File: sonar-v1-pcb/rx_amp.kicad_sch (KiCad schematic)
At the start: 13 parts, among them U301 Opamp_Dual

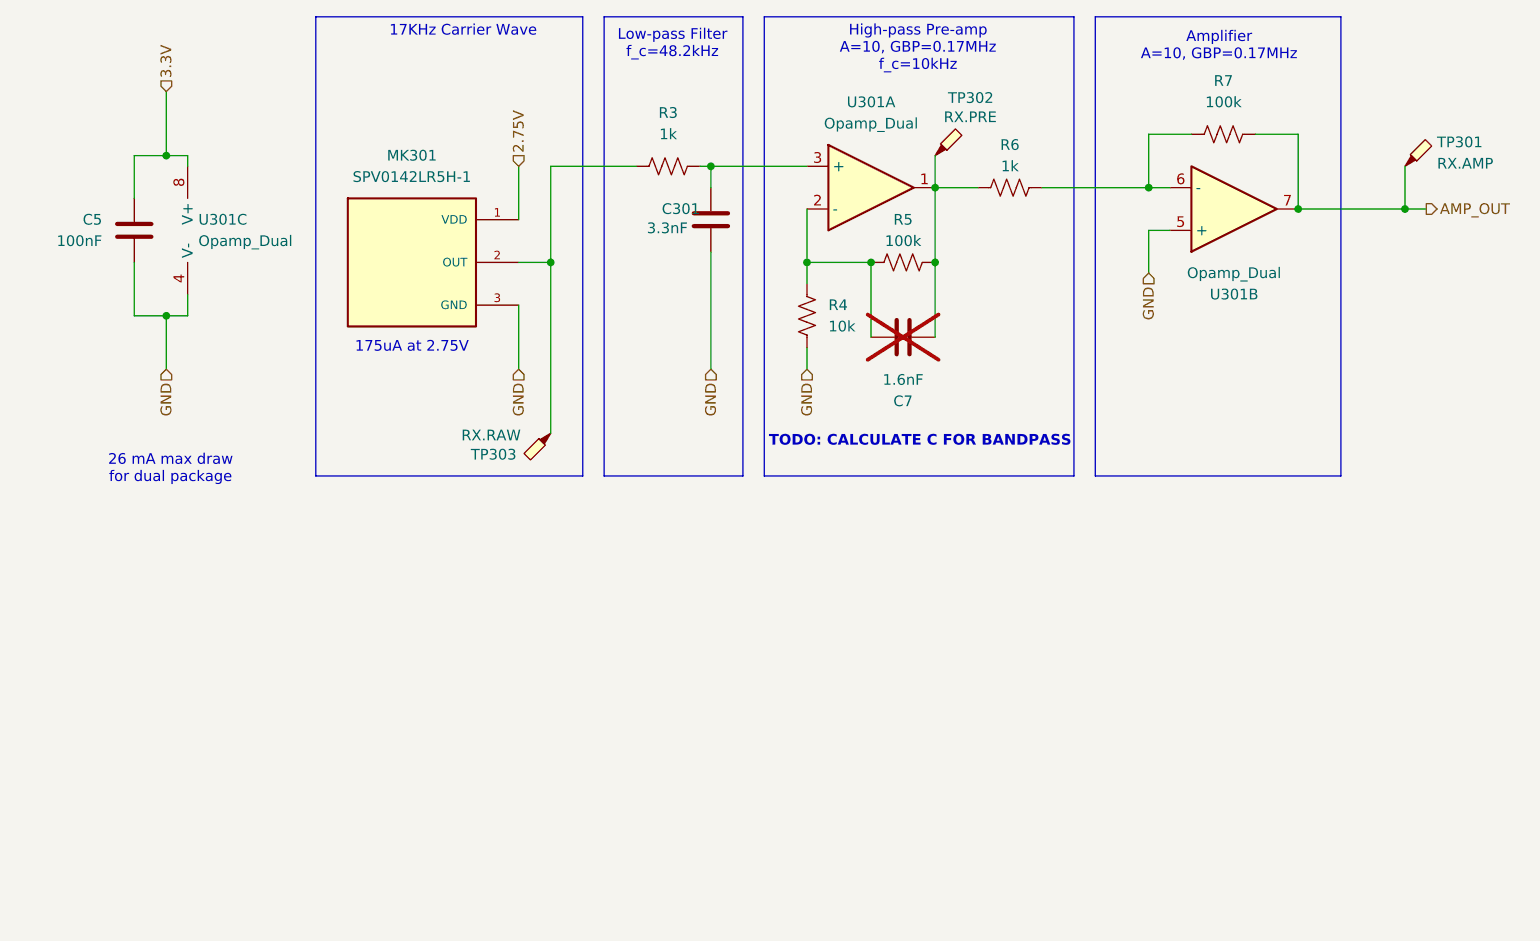
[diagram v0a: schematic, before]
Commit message: WIP hand-off: rx amp sim project, SPICE models, schematic updates
Adds rx_amp_sim KiCad project, SPICE models, Python setup-kicad.py
(replaces test_py.sh), CLAUDE.md, and a sweep of schematic edits across
the v1 board.

Co-Authored-By: Claude Opus 4.7 <noreply@anthropic.com>
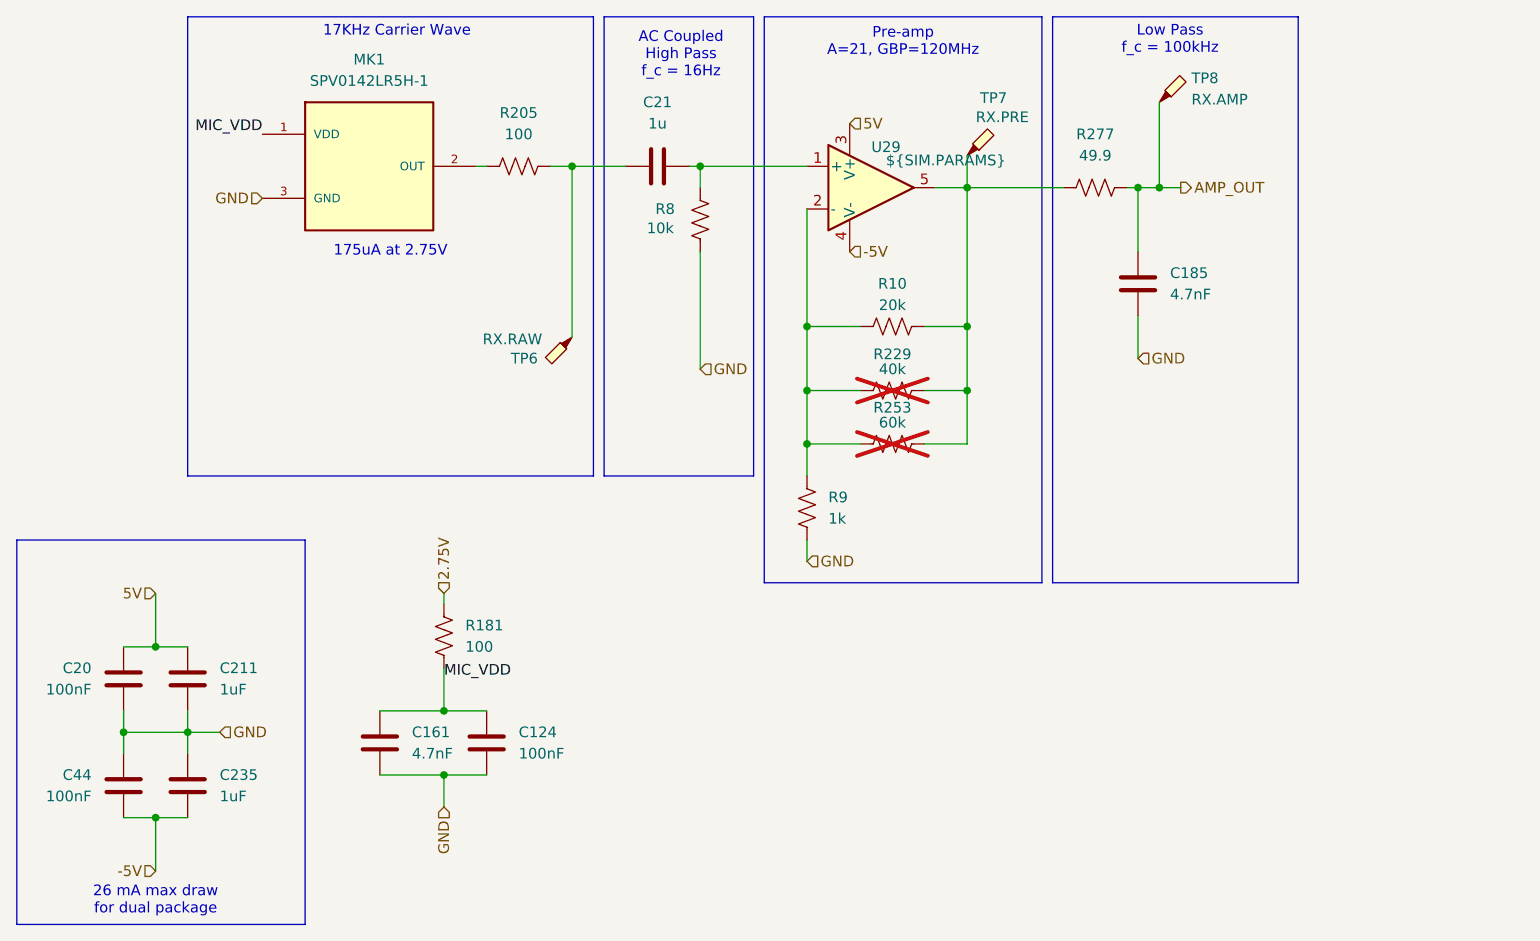
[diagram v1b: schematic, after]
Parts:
- removed C301: 3.3nF, Capacitor_SMD:C_0402_1005Metric, symbol Device:C
- removed C7: 1.6nF, GS_Capacitors:C_0603_1608Metric, symbol GS_Capacitor_0603:C_0603_1.6nF
- removed R3, R6: 1k, GS_Resistors:R_0603_1608Metric, symbol GS_Resistor_0603:R_0603_1k
- removed R7: 100k, GS_Resistors:R_0603_1608Metric, symbol GS_Resistor_0603:R_0603_100k
- removed U301: Opamp_Dual, Package_SO:TSSOP-8_3x3mm_P0.65mm, symbol Device:Opamp_Dual
- added C124: 100nF, Sonar:C_0603_1608Metric, symbol sonar_lib:C_0603_100nF
- added C161, C185: 4.7nF, Sonar:C_0603_1608Metric, symbol sonar_lib:C_0603_4.7nF
- added C21: 1u, symbol Device:C
- added C211, C235: 1uF, Sonar:C_0603_1608Metric, symbol sonar_lib:C_0603_4.7nF
- added C44: 100nF, GS_Capacitors:C_0603_1608Metric, symbol GS_Capacitor_0603:C_0603_100nF
- added R181, R205: 100, symbol Device:R_US
- added R229: 40k, GS_Resistors:R_0603_1608Metric, symbol GS_Resistor_0603:R_0603_100k
- added R253: 60k, GS_Resistors:R_0603_1608Metric, symbol GS_Resistor_0603:R_0603_100k
- added R277: 49.9, symbol Device:R_US
- added R8: 10k, symbol Device:R_US
- added U29: ${SIM.PARAMS}, Package_TO_SOT_SMD:SOT-23-5, symbol Simulation_SPICE:OPAMP
- MK1: renamed from MK301; symbol sonar_lib:SPV08A0LR5H-1 -> sonar_lib:SPV0142LR5H-1; MP SPV08A0LR5H-1 -> SPV0142LR5H-1
- R10: renamed from R5; value 100k -> 20k
- R9: renamed from R4; value 10k -> 1k
- renumbered C5 to C20, TP303 to TP6, TP302 to TP7, TP301 to TP8
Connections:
- net 2.75V: now also R181.1; no longer MK1.1 (VDD)
- net AMP_OUT: now also C185.1, R277.2
- net GND: now also C124.2, C161.2, C185.2, C211.2, C235.1, C44.1, R8.2
- net at TP6.1: now also C21.1, R205.2; no longer MK1.2 (OUT)
- net at R10.1, R9.1: now also R229.1, R253.1, U29.2 (-)
- net at R10.2, TP7.1: now also R229.2, R253.2, R277.1, U29.5
- net 3.3V renamed 5V
- net 5V: now also C211.1, U29.3 (V+)
- new net: C21.2, R8.1, U29.1 (+)
- new net: MK1.2 (OUT), R205.1
- new net -5V: C235.2, C44.2, U29.4 (V-)
- new net MIC_VDD: C124.1, C161.1, MK1.1 (VDD), R181.2
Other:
- note added: "AC Coupled High Pass f_c = 16Hz"
- note added: "Low Pass f_c = 100kHz"
- note added: "Pre-amp A=21, GBP=120MHz"
- note removed: "Amplifier A=10, GBP=0.17MHz"
- note removed: "High-pass Pre-amp A=10, GBP=0.17MHz f_c=10kHz"
- note removed: "Low-pass Filter f_c=48.2kHz"
- note removed: "TODO: CALCULATE C FOR BANDPASS"
- company: (none) -> Joshua Himmens & George Sleen
- moved on the sheet: C20, MK1, R10, R9, TP6, TP7, TP8

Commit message: Add quad RX pre-amp and MEMS RX sheets; RX amp rework
- New sub-sheets quad_rx_pre_amp and mems_rx added under the
  eight_transducer_array, with R_GAIN_HIGH/R_GAIN_TARGET project
  text variables to parameterize gain
- Substantial rework of rx_amp.kicad_sch
- rx_amp_sim: add OP analysis to the workbook
- Drop stale sonar.csv export
- Add .gitignore for KiCad user-local files (*.kicad_prl, ~*.lck,
  *-backups/, *.bak, fp-info-cache) and VS Code .history/

Co-Authored-By: Claude Opus 4.7 <noreply@anthropic.com>
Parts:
- removed C124: 100nF, Sonar:C_0603_1608Metric, symbol sonar_lib:C_0603_100nF
- removed C161: 4.7nF, Sonar:C_0603_1608Metric, symbol sonar_lib:C_0603_4.7nF
- removed R181: 100, symbol Device:R_US
- added C126: 100nF, Sonar:C_0603_1608Metric, symbol sonar_lib:C_0603_100nF
- added R301: 100, symbol Device:R_US
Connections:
- net 2.75V: now also C126.1, R301.1
- net GND: now also C126.2
- net MIC_VDD: no longer names the net of MK1.1 (VDD)
- net MIC_VDD: now also R301.2
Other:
- moved on the sheet: R8, TP6
